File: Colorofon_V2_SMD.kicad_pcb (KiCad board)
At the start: 2 copper layers, 104 x 94 mm, 94 parts, among them J1 Barrel_Jack_MountingPin, J2 AudioJack3, J3 691322310002, J4 691322310002, J5 691322310002, Q1 BC547, Q2 BC547, Q3 BC547, Q4 BD140, Q5 BD140, Q6 BD140, SW1 SW_Push, U1 LM358, U2 MCP6002-xP, U3 MCP6002-xP

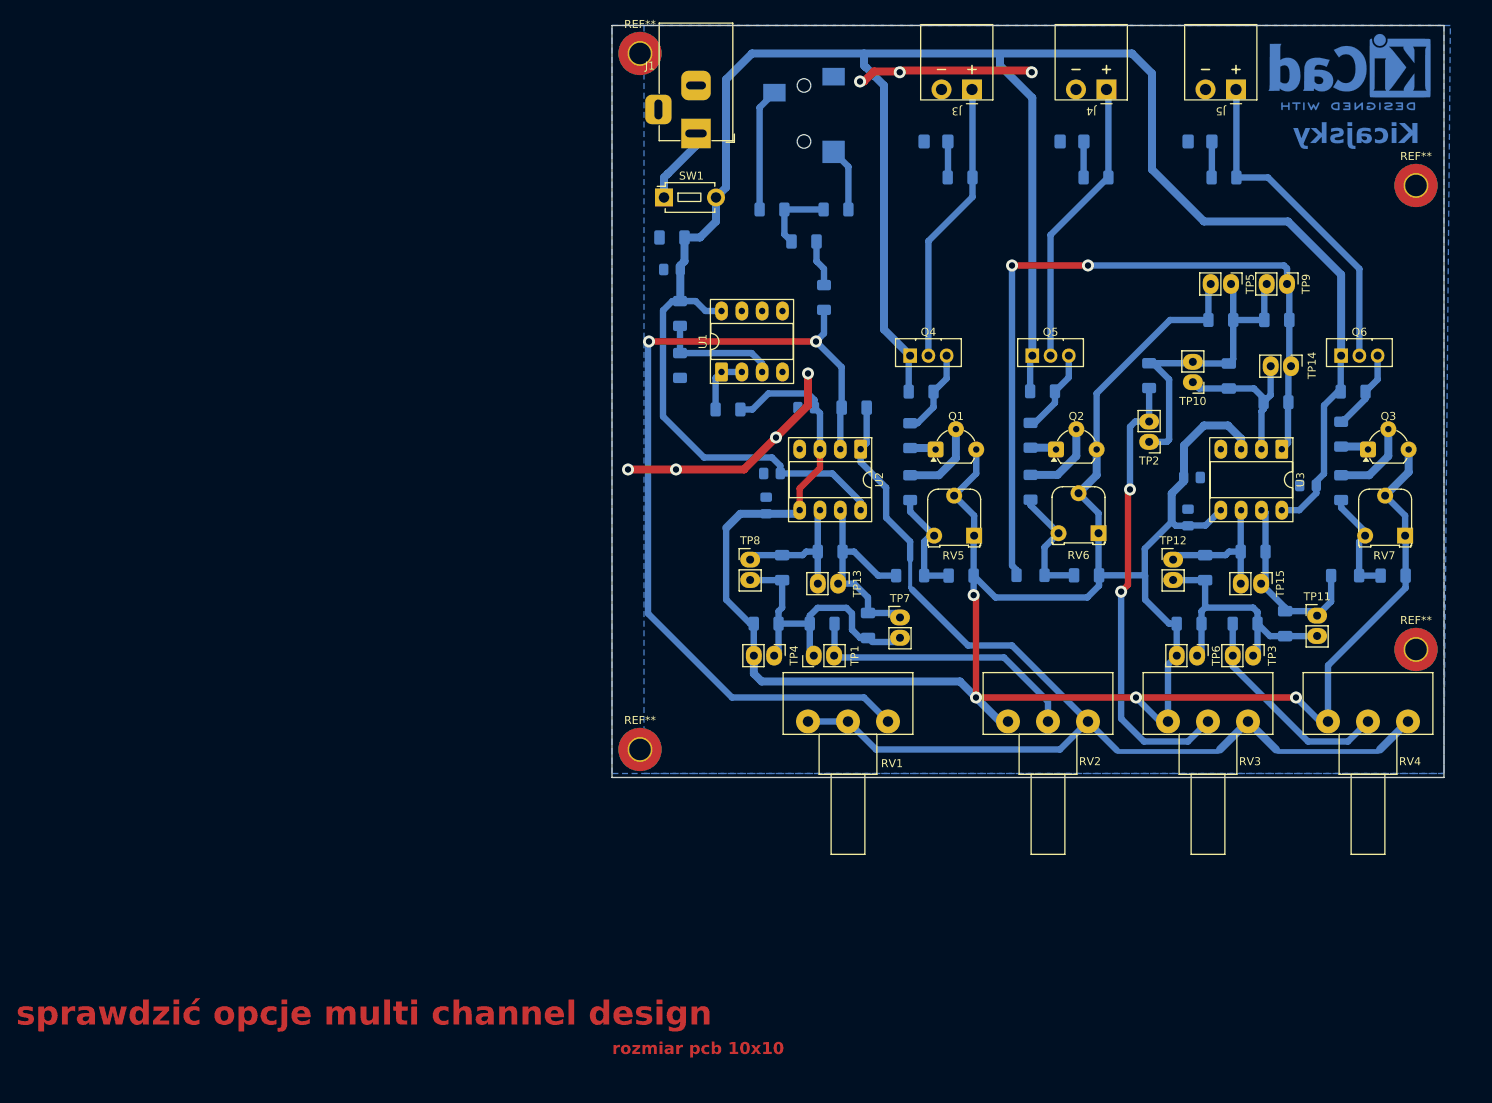
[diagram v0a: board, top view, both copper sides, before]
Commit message: Change filters components
main clean board layout
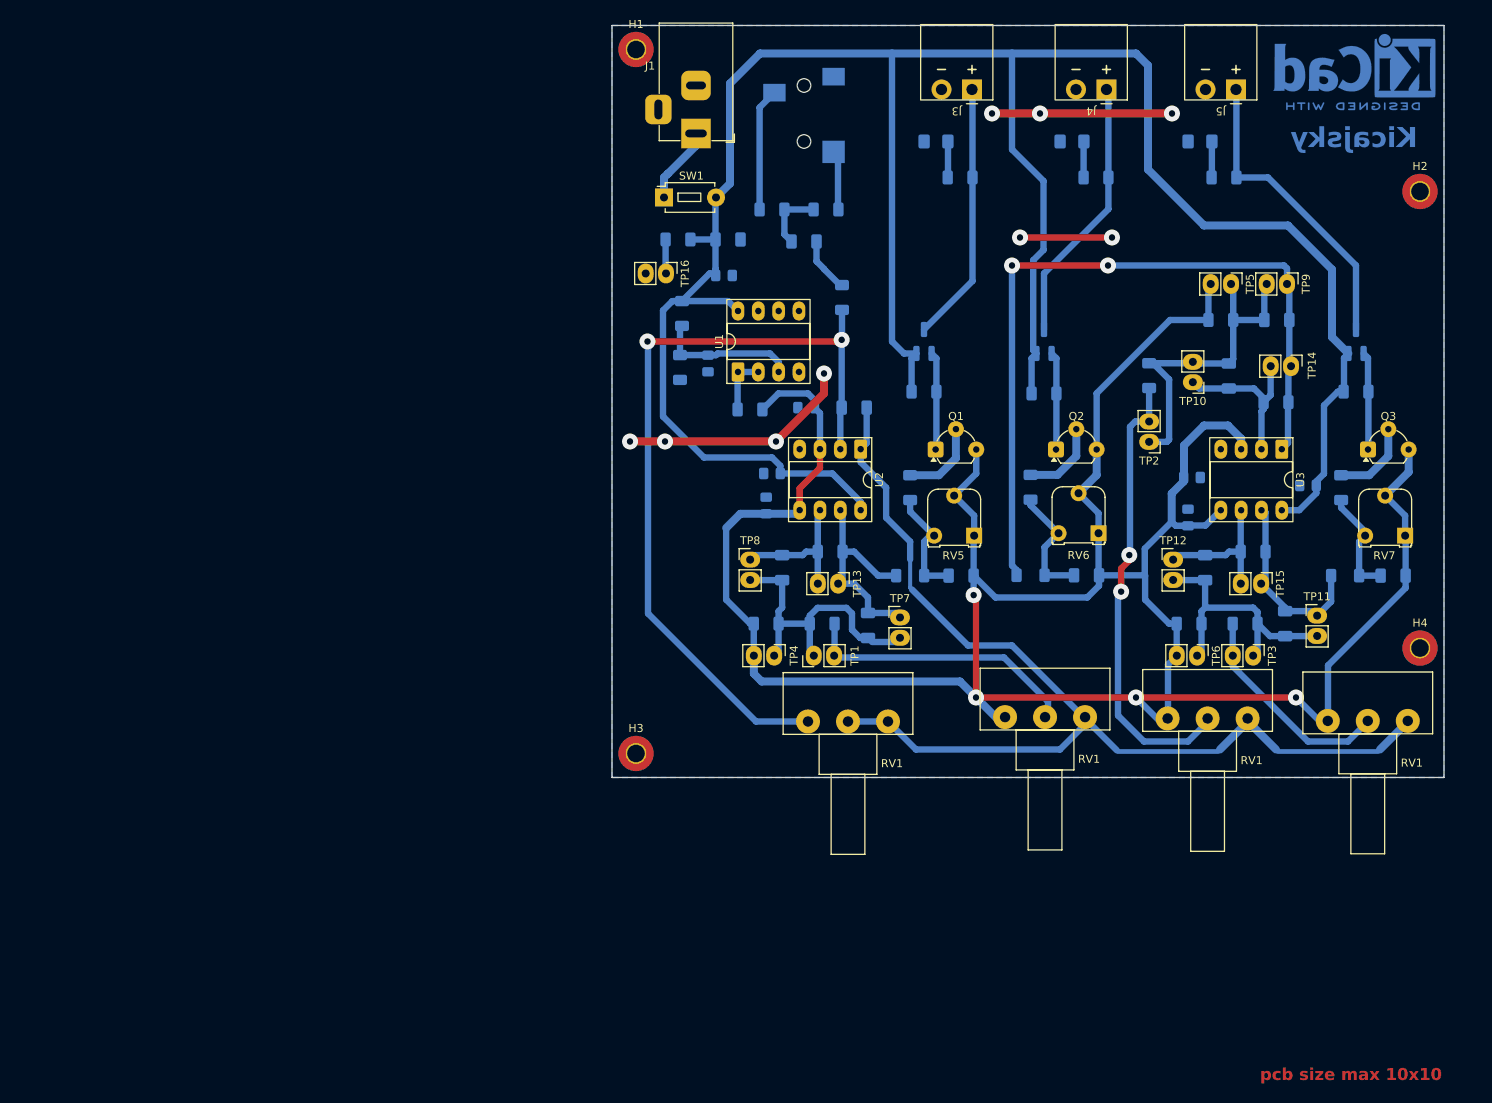
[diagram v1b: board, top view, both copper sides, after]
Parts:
- removed R20, R22, R24: 100, Resistor_SMD:R_1206_3216Metric_Pad1.30x1.75mm_HandSolder
- removed REF** (x4): MountingHole_2.7mm_Pad_TopBottom, MountingHole:MountingHole_2.7mm_Pad_TopBottom
- removed RV2, RV3, RV4: 100k, My_Library:Potentiometer_Piher_T-16H_Single_Horizontal
- added C20: 100n, Capacitor_SMD:C_0805_2012Metric_Pad1.18x1.45mm_HandSolder, B.Cu at (109.0, 90.2)
- added H1: MountingHole, MountingHole:MountingHole_2.2mm_M2_Pad_TopBottom, F.Cu at (100.0, 51.0)
- added H2: MountingHole, MountingHole:MountingHole_2.2mm_M2_Pad_TopBottom, F.Cu at (198.0, 68.8)
- added H3: MountingHole, MountingHole:MountingHole_2.2mm_M2_Pad_TopBottom, F.Cu at (100.0, 139.0)
- added H4: MountingHole, MountingHole:MountingHole_2.2mm_M2_Pad_TopBottom, F.Cu at (198.0, 125.8)
- added R28: 1,8k, Resistor_SMD:R_1206_3216Metric_Pad1.30x1.75mm_HandSolder, B.Cu at (105.2, 74.8)
- added RV1: 200k, My_Library:Potentiometer_Piher_T-16H_Single_Horizontal, F.Cu at (186.5, 134.9)
- added RV1: 200k, My_Library:Potentiometer_Piher_T-16H_Single_Horizontal, F.Cu at (146.1, 134.4)
- added RV1: 200k, My_Library:Potentiometer_Piher_T-16H_Single_Horizontal, F.Cu at (166.4, 134.6)
- added TP16: ~, My_Library:PinHeader_1x02_P2.54mm_Vertical_Hand_Solder, F.Cu at (103.8, 79.0)
- C10, C11: value 22n -> 4,7n
- C12, C13: value 22n -> 680p
- Q4, Q5, Q6: value BD140 -> PMV65XP; footprint Package_TO_SOT_THT:TO-126-3_Vertical -> Package_TO_SOT_SMD:SOT-23_Handsoldering; moved to B.Cu
- R11: value 100k -> 1k
- R12: value 100k -> 560
- R13: value 510k -> 1M
- R14: value 510k -> 220k
- R15: value 510k -> 470k
- R7: value 100k -> 56k
- R8: value 100k -> 15k
- R9: value 100k -> 27k
- RV1: value 100k -> 200k
- moved C1 7.00 mm to (111.5, 74.8), turned to 0 degrees
- moved C2 6.54 mm to (111.0, 79.2), turned to 180 degrees
- moved R3 2.75 mm to (114.2, 96.0)
- moved Q6 2.57 mm to (190.0, 87.5), turned to 90 degrees
- moved Q4 2.48 mm to (136.0, 87.5), turned to 90 degrees
- moved Q5 2.30 mm to (151.0, 87.5), turned to 90 degrees
- moved R6 2.25 mm to (125.8, 82.0)
- moved U1 2.06 mm to (112.8, 91.3)
- moved R4 1.25 mm to (123.8, 71.0)
- moved SYM1 0.61 mm to (189.8, 53.0)
- moved R19 0.36 mm to (136.0, 93.8)
- moved R23 0.36 mm to (190.0, 93.8)
- moved R21 0.33 mm to (151.0, 94.0)
- moved R1 0.25 mm to (105.8, 84.0)
- moved R2 0.25 mm to (105.5, 90.8)
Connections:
- J3 pad 1: Net-(Q4-C) -> Net-(Q4-D)
- J4 pad 1: Net-(Q5-C) -> Net-(Q5-D)
- J5 pad 1: Net-(Q6-C) -> Net-(Q6-D)
- Q4 pad 1: +12V -> Net-(Q1-C)
- Q4 pad 2: Net-(Q4-C) -> +12V
- Q4 pad 3: Net-(Q4-B) -> Net-(Q4-D)
- Q5 pad 1: +12V -> Net-(Q2-C)
- Q5 pad 2: Net-(Q5-C) -> +12V
- Q5 pad 3: Net-(Q5-B) -> Net-(Q5-D)
- Q6 pad 1: +12V -> Net-(Q3-C)
- Q6 pad 2: Net-(Q6-C) -> +12V
- Q6 pad 3: Net-(Q6-B) -> Net-(Q6-D)
- R19 pad 1: Net-(Q4-B) -> Net-(Q1-C)
- R21 pad 1: Net-(Q5-B) -> Net-(Q2-C)
- R23 pad 1: Net-(Q6-B) -> Net-(Q3-C)
- R25 pad 1: Net-(Q4-C) -> Net-(Q4-D)
- R26 pad 1: Net-(Q5-C) -> Net-(Q5-D)
- R27 pad 1: Net-(Q6-C) -> Net-(Q6-D)
- RV1 pad 1: Net-(C6-Pad2) -> Net-(U2A--)
- RV1 pad 3: Net-(U2A--) -> Net-(C6-Pad2)
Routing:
- net Net-(Q6-C): track 41.9 -> 0.00 mm
- net Net-(Q6-D): track 0.00 -> 38.5 mm
- net Net-(Q5-C): track 36.0 -> 0.00 mm
- net Net-(Q4-C): track 35.5 -> 0.00 mm
- net Net-(Q5-D): track 0.00 -> 33.1 mm
- net Net-(Q4-D): track 0.00 -> 32.4 mm
- net GND: track 52.3 -> 63.4 mm, vias 7 -> 9
- net Net-(Q4-B): track 10.9 -> 0.00 mm
- net Net-(Q5-B): track 10.7 -> 0.00 mm
- net Net-(Q6-B): track 10.3 -> 0.00 mm
- net Net-(Q2-C): track 2.96 -> 12.3 mm
- net Net-(Q3-C): track 3.00 -> 12.3 mm
- net Net-(Q1-C): track 3.15 -> 12.3 mm
- net +12V: track 300.8 -> 309.5 mm
- net Net-(U2A--): track 109.5 -> 101.3 mm
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- removed copper zone on B.Cu, net (none)
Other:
- board text added: "pcb size max 10x10"
- board text removed: "rozmiar pcb 10x10"
- board text removed: "sprawdzić opcje multi channel design"

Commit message: Update layout
Final layout for version 2
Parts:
- removed R3: 0/10, Resistor_SMD:R_1206_3216Metric_Pad1.30x1.75mm_HandSolder
- removed the RV1 at (186.5, 134.9)
- removed the RV1 at (146.1, 134.4)
- removed the RV1 at (166.4, 134.6)
- removed SW1: SW_Push, Button_Switch_THT:SW_PUSH_1P1T_6x3.5mm_H4.3_APEM_MJTP1243
- removed SYM1: SYM_EasterEgg_42x60mm, Symbol:KiCad-Logo2_8mm_Copper
- removed TP1, TP10, TP11, TP12, TP13, TP14, TP15, TP16, TP2, TP3, TP4, TP5, TP6, TP7, TP8, TP9: ~, My_Library:PinHeader_1x02_P2.54mm_Vertical_Hand_Solder
- added J6: Conn_01x02_Pin, My_Footprints:PinHeader_1x02_P2.54mm_Vertical_Hand_Solder, F.Cu at (106.7, 80.8)
- added R20: 10, Resistor_SMD:R_1206_3216Metric_Pad1.30x1.75mm_HandSolder, B.Cu at (130.5, 122.2)
- added R22: 1k, Resistor_SMD:R_1206_3216Metric_Pad1.30x1.75mm_HandSolder, B.Cu at (178.8, 115.0)
- added R24: 1k, Resistor_SMD:R_1206_3216Metric_Pad1.30x1.75mm_HandSolder, B.Cu at (182.2, 98.4)
- added R29: 1k, Resistor_SMD:R_1206_3216Metric_Pad1.30x1.75mm_HandSolder, B.Cu at (126.0, 114.8)
- added R30: 10, Resistor_SMD:R_1206_3216Metric_Pad1.30x1.75mm_HandSolder, B.Cu at (153.8, 113.8)
- added R31: 10, Resistor_SMD:R_1206_3216Metric_Pad1.30x1.75mm_HandSolder, B.Cu at (186.0, 121.2)
- added R32: 10, Resistor_SMD:R_1206_3216Metric_Pad1.30x1.75mm_HandSolder, B.Cu at (117.2, 97.5)
- added REF**: KiCad-Logo2_8mm_Copper, Symbol:KiCad-Logo2_8mm_Copper, F.Cu at (192.8, 55.0)
- added RV2: 1k, My_Footprints:Potentiometer_Piher_T-16H_Single_Horizontal, F.Cu at (149.1, 137.0)
- added RV3: 1k, My_Footprints:Potentiometer_Piher_T-16H_Single_Horizontal, F.Cu at (169.4, 137.1)
- added RV4: 1k, My_Footprints:Potentiometer_Piher_T-16H_Single_Horizontal, F.Cu at (189.5, 137.1)
- added SW2: SW_SPDT, My_Footprints:SW_Toggle_Blue_wSlots, F.Cu at (111.0, 70.5)
- C10: value 4,7n -> 680p
- C11: value 4,7n -> 1n
- C12: value 680p -> 100p
- C13: value 680p -> 4,7n
- C17, C18, C19: value 4.7u -> 10u
- C8: value 22n -> 10n
- C9: value 22n -> 33n
- H1, H2, H3, H4: footprint MountingHole:MountingHole_2.2mm_M2_Pad_TopBottom -> MountingHole:MountingHole_2.2mm_M2
- J1: footprint My_Library:BarrelJack_Horizontal -> My_Footprints:BarrelJack_Horizontal
- J2: value AudioJack3 -> AudioJack3_SwitchTR; footprint Connector_Audio:Jack_3.5mm_CUI_SJ-3523-SMT_Horizontal -> My_Footprints:Jack_3.5mm_CUI_SJ2-3593D-SMT_Horizontal
- J3, J4, J5: value 691322310002 -> Connector 1x2 WE 691322310002; footprint My_Library:J_Wurth_WR-TBL_691322310002 -> My_Footprints:J_Wurth_WR-TBL_691322310002
- Q1, Q2, Q3: value BC547 -> BC847; footprint My_Library:TO-92L_Wide_Hand -> Package_TO_SOT_SMD:SOT-23; moved to B.Cu
- Q4, Q5, Q6: footprint Package_TO_SOT_SMD:SOT-23_Handsoldering -> Package_TO_SOT_SMD:SOT-23
- R11: value 1k -> 10k
- R13: value 1M -> 560k
- R14: value 220k -> 660k
- R4, R5, R6: value 5.1k -> 5,1k
- R7: value 56k -> 1k
- R8: value 15k -> 1k
- R9: value 27k -> 1k
- RV1: value 200k -> 100k; footprint My_Library:Potentiometer_Piher_T-16H_Single_Horizontal -> My_Footprints:Potentiometer_Piher_T-16H_Single_Horizontal
- RV5, RV6, RV7: footprint My_Library:Potentiometer_Runtron_RM-065_Vertical_Hand_Solder -> My_Footprints:Potentiometer_Runtron_RM-065_Vertical_Hand_Solder
- U2, U3: value MCP6002-xP -> LM358
- moved R17 12.7 mm to (162.0, 104.8), turned to 0 degrees
- moved Q5 11.0 mm to (162.0, 87.5)
- moved Q2 10.8 mm to (163.0, 98.3), turned to 90 degrees
- moved R21 10.5 mm to (161.5, 93.0)
- moved C15 9.82 mm to (177.2, 98.4), turned to 0 degrees
- moved R16 8.54 mm to (142.8, 104.8), turned to 0 degrees
- moved C3 7.93 mm to (128.8, 76.5)
- moved R7 7.92 mm to (130.5, 126.0)
- moved R8 7.89 mm to (172.0, 92.5), turned to 0 degrees
- moved R5 7.60 mm to (122.3, 76.5)
- moved C18 7.05 mm to (163.1, 118.8)
- moved RV6 7.05 mm to (164.6, 113.5)
- moved Q1 6.87 mm to (143.8, 98.2), turned to 90 degrees
- moved Q4 6.75 mm to (142.8, 87.5)
- moved D2 6.50 mm to (155.5, 118.8)
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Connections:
- C10 pad 1: Net-(D2-A) -> Net-(C10-Pad1)
- C12 pad 1: Net-(D3-A) -> Net-(C12-Pad1)
- C8 pad 1: Net-(D1-A) -> Net-(C8-Pad1)
- Q1 pad 1: Net-(Q1-C) -> Net-(Q1-B)
- Q1 pad 2: Net-(Q1-B) -> /Vref
- Q1 pad 3: /Vref -> Net-(Q1-C)
- Q2 pad 1: Net-(Q2-C) -> Net-(Q2-B)
- Q2 pad 2: Net-(Q2-B) -> /Vref
- Q2 pad 3: /Vref -> Net-(Q2-C)
- Q3 pad 1: Net-(Q3-C) -> Net-(Q3-B)
- Q3 pad 2: Net-(Q3-B) -> /Vref
- Q3 pad 3: /Vref -> Net-(Q3-C)
- R13 pad 2: Net-(D1-A) -> Net-(C8-Pad1)
- R14 pad 2: Net-(D2-A) -> Net-(C10-Pad1)
- R15 pad 2: Net-(D3-A) -> Net-(C12-Pad1)
- U1 pad 5: unconnected-(U1B-+-Pad5) -> GND
- U1 pad 6: unconnected-(U1B---Pad6) -> GND
- U2 pad 7: Net-(D1-A) -> Net-(C8-Pad1)
- U3 pad 1: Net-(D2-A) -> Net-(C10-Pad1)
- U3 pad 7: Net-(D3-A) -> Net-(C12-Pad1)
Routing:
- net Net-(D2-A): track 95.5 -> 3.43 mm, vias 2 -> 0
- net Net-(C10-Pad1): track 0.00 -> 78.8 mm, vias 0 -> 2
- net GND: track 63.4 -> 0.00 mm, vias 9 -> 8
- net Net-(C10-Pad2): track 40.6 -> 11.4 mm
- net Net-(C8-Pad2): track 36.6 -> 10.8 mm
- net Net-(C12-Pad2): track 34.4 -> 11.0 mm
- net Net-(D1-A): track 27.7 -> 6.21 mm
- net Net-(D3-A): track 24.2 -> 3.22 mm
- net Net-(U2A--): track 101.3 -> 81.2 mm
- net Net-(C12-Pad1): track 0.00 -> 17.0 mm
- net /Vref: track 336.4 -> 320.2 mm, vias 4 -> 8
- net Net-(C8-Pad1): track 0.00 -> 15.6 mm
- net +12V: track 309.5 -> 295.9 mm, vias 0 -> 2
- net Net-(J2-PadR): track 15.4 -> 23.5 mm
- net Net-(J2-PadT): track 6.35 -> 13.8 mm
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- added copper zone on F.Cu, net GND
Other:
- board size 104 x 94 mm -> 104 x 95 mm
